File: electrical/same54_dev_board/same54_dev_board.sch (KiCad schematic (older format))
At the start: 0 parts

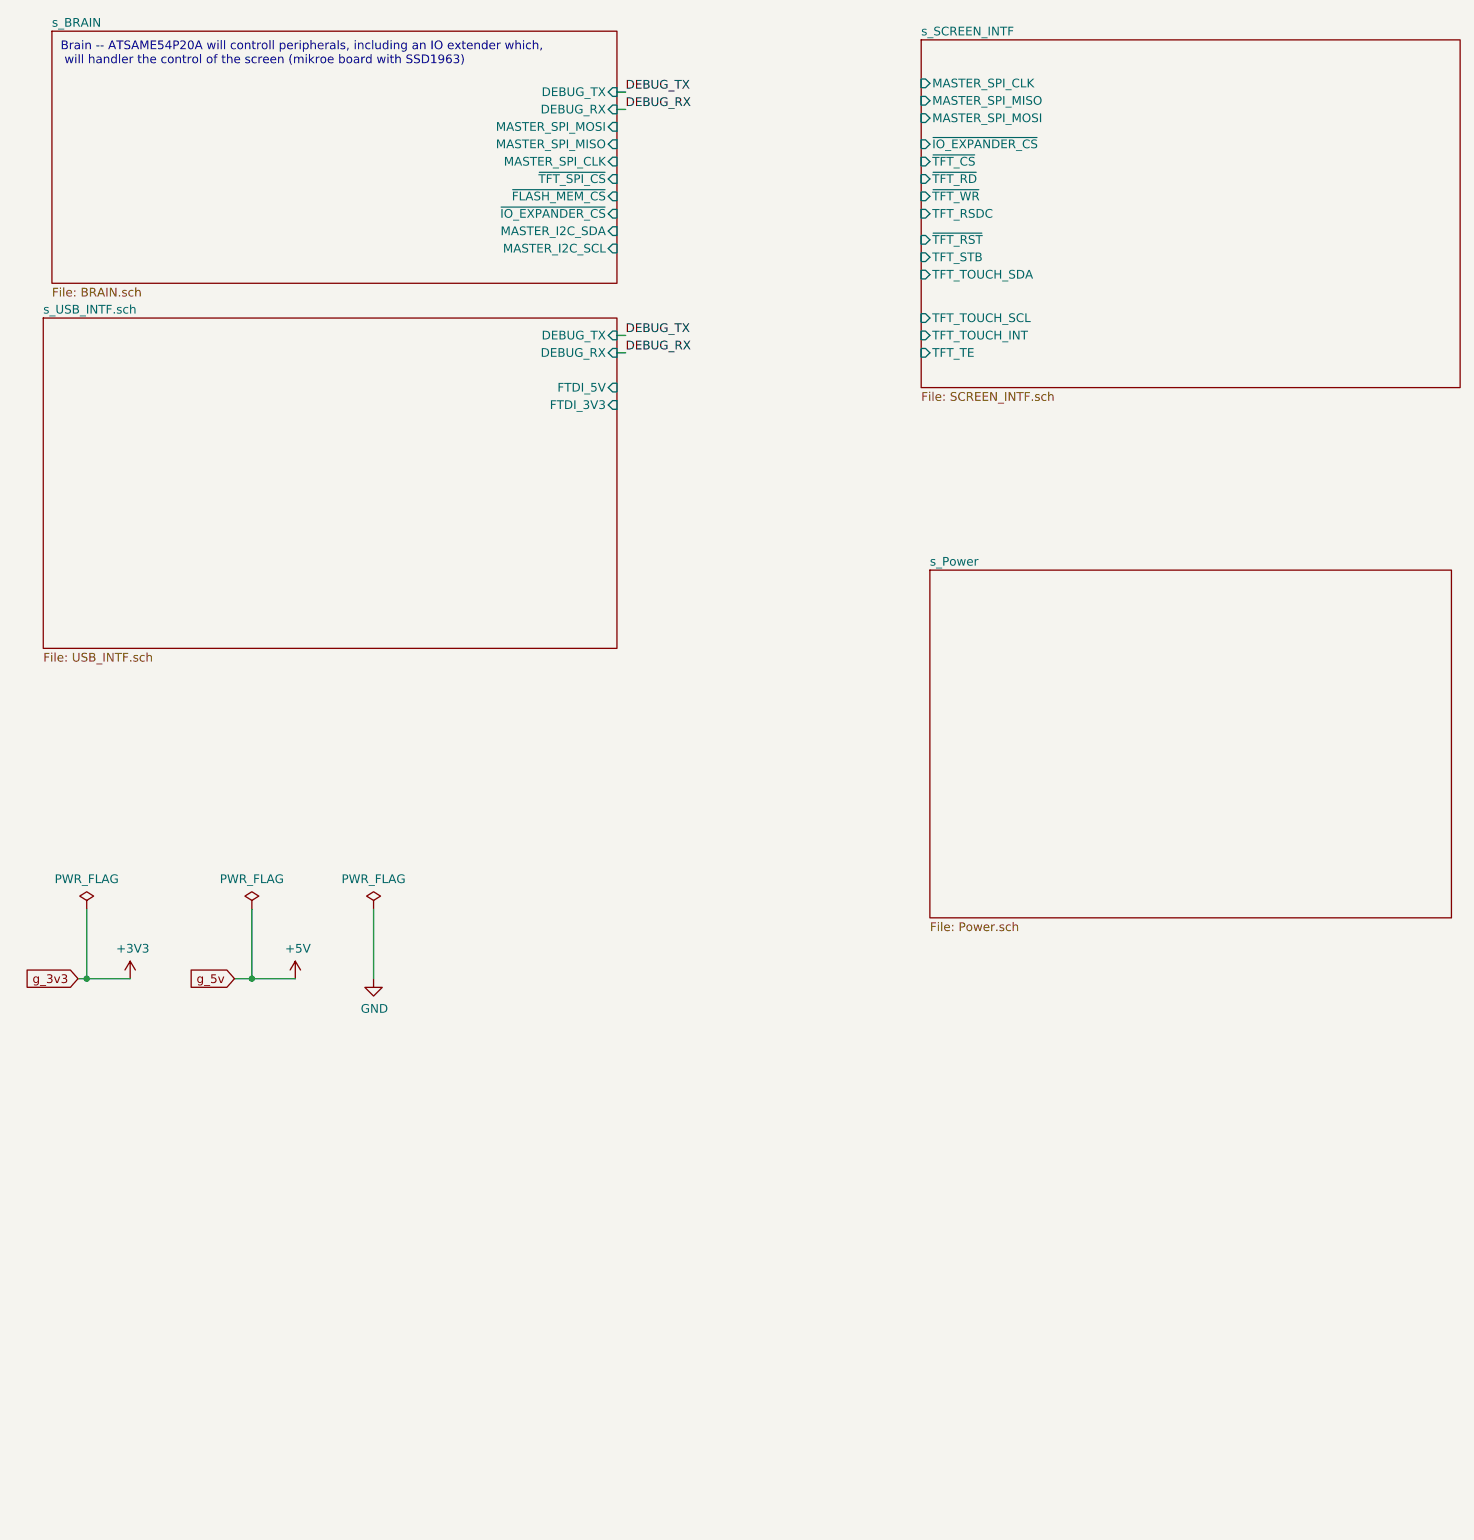
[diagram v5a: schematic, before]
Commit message: Added usart, i2c, and spi pin locations, as well as labeled sercoms
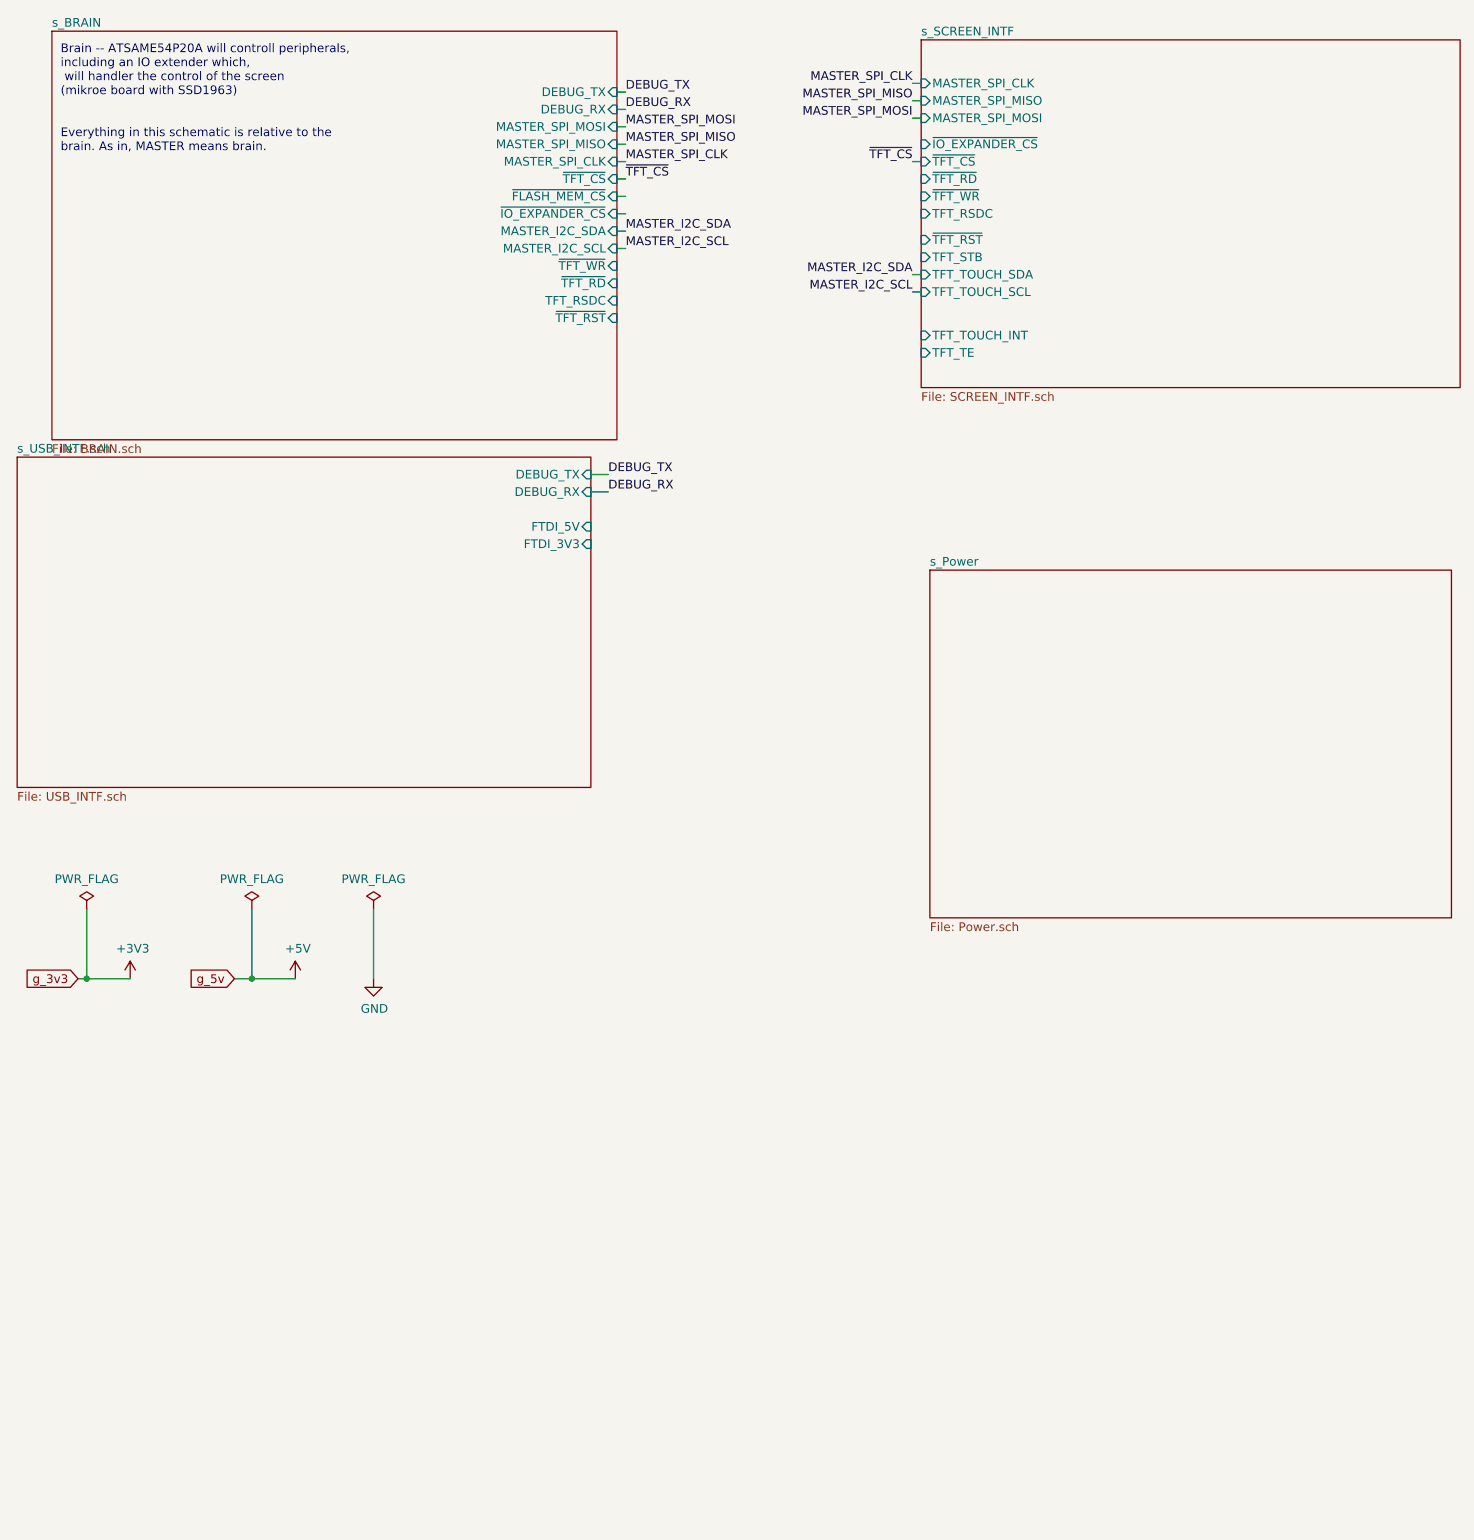
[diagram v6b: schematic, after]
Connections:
- net labels added: MASTER_I2C_SCL, MASTER_I2C_SDA, MASTER_SPI_CLK, MASTER_SPI_MISO, MASTER_SPI_MOSI, ~TFT_CS
- wire segments 11 -> 25
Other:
- note added: "Brain -- ATSAME54P20A will controll peripherals, \nincluding an IO extender which,\n will handler the control of the screen \n(mikroe board with SSD1963)\n\n\nEverything in this schematic is relative to the \nbrain. As in, MASTER means brain."
- note removed: "Brain -- ATSAME54P20A will controll peripherals, including an IO extender which,\n will handler the control of the screen (mikroe board with SSD1963)"
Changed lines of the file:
@@
 F1 "Power.sch" 50
 $EndSheet
-$Sheet
-S 700  2450 3300 1900
-U 5E7C0F59
-F0 "s_USB_INTF.sch" 50
-F1 "USB_INTF.sch" 50
-F2 "DEBUG_TX" I R 4000 2550 50
-F3 "DEBUG_RX" I R 4000 2650 50
-F4 "FTDI_5V" I R 4000 2850 50
-F5 "FTDI_3V3" I R 4000 2950 50
-$EndSheet
-$Sheet
-S 750  800  3250 1450
-U 5E805E4F
-F0 "s_BRAIN" 50
-F1 "BRAIN.sch" 50
-F2 "DEBUG_TX" I R 4000 1150 50
-F3 "DEBUG_RX" I R 4000 1250 50
-F4 "MASTER_SPI_MOSI" I R 4000 1350 50
-F5 "MASTER_SPI_MISO" I R 4000 1450 50
-F6 "MASTER_SPI_CLK" I R 4000 1550 50
-F7 "~TFT_SPI_CS" I R 4000 1650 50
-F8 "~FLASH_MEM_CS" I R 4000 1750 50
-F9 "MASTER_I2C_SDA" I R 4000 1950 50
-F10 "MASTER_I2C_SCL" I R 4000 2050 50
-F11 "~IO_EXPANDER_CS" I R 4000 1850 50
-$EndSheet
-Text Notes 800  1000 0    50   ~ 0
-Brain -- ATSAME54P20A will controll peripherals, including an IO extender which,\n will handler the control of the screen (mikroe board with SSD1963)
+Text Notes 800  1500 0    50   ~ 0
+Brain -- ATSAME54P20A will controll peripherals, \nincluding an IO extender which,\n will handler the control of the screen \n(mikroe board with SSD1963)\n\n\nEverything in this schematic is relative to the \nbrain. As in, MASTER means brain.
 Text GLabel 900  6250 0    50   Input ~ 0
 g_3v3
@@
 F11 "TFT_STB" I L 5750 2100 50
 F12 "TFT_TOUCH_SDA" I L 5750 2200 50
-F13 "TFT_TOUCH_SCL" I L 5750 2450 50
+F13 "TFT_TOUCH_SCL" I L 5750 2300 50
 F14 "TFT_TOUCH_INT" I L 5750 2550 50
 F15 "TFT_TE" I L 5750 2650 50
@@
 Wire Wire Line
 	4000 1150 4050 1150
-Text Label 4050 2550 0    50   ~ 0
-DEBUG_TX
 Wire Wire Line
 	4000 1250 4050 1250
@@
 DEBUG_RX
 Wire Wire Line
-	4000 2550 4050 2550
-Wire Wire Line
-	4000 2650 4050 2650
-Text Label 4050 2650 0    50   ~ 0
+	4000 1350 4050 1350
+Wire Wire Line
+	4000 1450 4050 1450
+Wire Wire Line
+	4000 1550 4050 1550
+Wire Wire Line
+	4000 1650 4050 1650
+Wire Wire Line
+	4000 1750 4050 1750
+Wire Wire Line
+	4000 1850 4050 1850
+Wire Wire Line
+	4000 1950 4050 1950
+Wire Wire Line
+	4000 2050 4050 2050
+Text Label 4050 1350 0    50   ~ 0
+MASTER_SPI_MOSI
+Text Label 4050 1450 0    50   ~ 0
+MASTER_SPI_MISO
+Text Label 4050 1550 0    50   ~ 0
+MASTER_SPI_CLK
+Text Label 4050 1650 0    50   ~ 0
+~TFT_CS
+Text Label 5700 1300 2    50   ~ 0
+MASTER_SPI_MOSI
+Wire Wire Line
+	5700 1200 5750 1200
+Text Label 5700 1200 2    50   ~ 0
+MASTER_SPI_MISO
+Wire Wire Line
+	5700 1300 5750 1300
+Text Label 5700 1100 2    50   ~ 0
+MASTER_SPI_CLK
+Wire Wire Line
+	5700 1100 5750 1100
+Text Label 5700 1550 2    50   ~ 0
+~TFT_CS
+Wire Wire Line
+	5700 1550 5750 1550
+Text Label 4050 1950 0    50   ~ 0
+MASTER_I2C_SDA
+Text Label 4050 2050 0    50   ~ 0
+MASTER_I2C_SCL
+Text Label 5700 2200 2    50   ~ 0
+MASTER_I2C_SDA
+Text Label 5700 2300 2    50   ~ 0
+MASTER_I2C_SCL
+Wire Wire Line
+	5750 2200 5700 2200
+Wire Wire Line
+	5750 2300 5700 2300
+Wire Wire Line
+	3850 3450 3950 3450
+Wire Wire Line
+	3850 3350 3950 3350
+Text Label 3950 3450 0    50   ~ 0
 DEBUG_RX
+Text Label 3950 3350 0    50   ~ 0
+DEBUG_TX
+$Sheet
+S 550  3250 3300 1900
+U 5E7C0F59
+F0 "s_USB_INTF.sch" 50
+F1 "USB_INTF.sch" 50
+F2 "DEBUG_TX" I R 3850 3350 50
+F3 "DEBUG_RX" I R 3850 3450 50
+F4 "FTDI_5V" I R 3850 3650 50
+F5 "FTDI_3V3" I R 3850 3750 50
+$EndSheet
+$Sheet
+S 750  800  3250 2350
+U 5E805E4F
+F0 "s_BRAIN" 50
+F1 "BRAIN.sch" 50
+F2 "DEBUG_TX" I R 4000 1150 50
+F3 "DEBUG_RX" I R 4000 1250 50
+F4 "MASTER_SPI_MOSI" I R 4000 1350 50
+F5 "MASTER_SPI_MISO" I R 4000 1450 50
+F6 "MASTER_SPI_CLK" I R 4000 1550 50
+F7 "~FLASH_MEM_CS" I R 4000 1750 50
+F8 "MASTER_I2C_SDA" I R 4000 1950 50
+F9 "MASTER_I2C_SCL" I R 4000 2050 50
+F10 "~IO_EXPANDER_CS" I R 4000 1850 50
+F11 "~TFT_CS" I R 4000 1650 50
+F12 "~TFT_WR" I R 4000 2150 50
+F13 "~TFT_RD" I R 4000 2250 50
+F14 "TFT_RSDC" I R 4000 2350 50
+F15 "~TFT_RST" I R 4000 2450 50
+$EndSheet
 $EndSCHEMATC

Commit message: migrating to laptop
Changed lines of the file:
@@
 	5750 2300 5700 2300
 Wire Wire Line
-	3850 3450 3950 3450
+	3950 3550 4050 3550
 Wire Wire Line
-	3850 3350 3950 3350
-Text Label 3950 3450 0    50   ~ 0
+	3950 3450 4050 3450
+Text Label 4050 3550 0    50   ~ 0
 DEBUG_RX
-Text Label 3950 3350 0    50   ~ 0
+Text Label 4050 3450 0    50   ~ 0
 DEBUG_TX
 $Sheet
-S 550  3250 3300 1900
+S 650  3350 3300 1900
 U 5E7C0F59
 F0 "s_USB_INTF.sch" 50
 F1 "USB_INTF.sch" 50
-F2 "DEBUG_TX" I R 3850 3350 50
-F3 "DEBUG_RX" I R 3850 3450 50
-F4 "FTDI_5V" I R 3850 3650 50
-F5 "FTDI_3V3" I R 3850 3750 50
+F2 "DEBUG_TX" I R 3950 3450 50
+F3 "DEBUG_RX" I R 3950 3550 50
+F4 "FTDI_5V" I R 3950 3750 50
+F5 "FTDI_3V3" I R 3950 3850 50
 $EndSheet
 $Sheet
